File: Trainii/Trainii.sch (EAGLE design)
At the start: 29 parts, among them J1 apd, J2 left motor encoder, J3 right motor encoder, J4 line sensor 2, J5 line sensor 1, J6 ultrasonic, J7 left motor output, J8 right motor output, J9 lift motor output

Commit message: Changed a few parts, corrected small wiring connections, routed board
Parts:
- removed U$1, U$2: DRV8833, Tranii:DRV8833
- removed U$8: BSS138, Tranii:BSS138
- removed U$9: LM3671, Tranii:LM3671
- added MC1, MC2: DRV8833, Trainii:DRV8833
- added U1: TPS61222DCKR, Trainii:TPS61222DCKR
- added U2: BSS138, Trainii:BSS138
- C2: value 0.1uF -> 10µF
- C3: value 10µF -> 0.1uF
- C5: value 4.7uF -> 10uF
- U$12: device Tranii:VLS3012HBX -> Trainii:VLS3012HBX
- U$6: device Tranii:ESP32 -> Trainii:ESP32
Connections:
- net OUT1 renamed LINE_OUT_1
- net OUT2 renamed LINE_OUT_2
- net TICKLEFT renamed TICK_LEFT
- net TICKRIGHT renamed TICK_RIGHT
- removed net LEFT0: J7.1, U$1.AOUT2
- removed net LEFT1: J7.2, U$1.AOUT1
- removed net LIFT0: J9.1, U$2.AOUT1
- removed net LIFT1: J9.2, U$2.AOUT2
- removed net N$2: C6.1, U$12.P$2, U$9.FB
- removed net RIGHT0: J8.1, U$1.BOUT1
- removed net RIGHT1: J8.2, U$1.BOUT2
- removed net VCC5: J6.1, R6.1
- new net +5V: C6.1, J6.1, R6.1, U1.FB, U1.VOUT
- new net LEFT_0: J7.1, MC1.AOUT1
- new net LEFT_1: J7.2, MC1.AOUT2
- new net LIFT_0: J9.1, MC2.AOUT1
- new net LIFT_1: J9.2, MC2.AOUT2
- new net RIGHT_0: J8.1, MC1.BOUT1
- new net RIGHT_1: J8.2, MC1.BOUT2
- net GND: now also C2.2, MC1.GND, MC1.PGND, MC2.GND, MC2.PGND, U1.GND; no longer C3.2, U$1.GND, U$1.PGND, U$2.GND, U$2.PGND, U$9.GND
- net LEFT_A: now also MC1.AIN1; no longer U$1.AIN1
- net LEFT_B: now also MC1.AIN2; no longer U$1.AIN2
- net LIFT_A: now also MC2.AIN1; no longer U$2.AIN1
- net LIFT_B: now also MC2.AIN2; no longer U$2.AIN2
- net N$1: now also U1.L; no longer U$9.SW
- net N$10: now also MC1.AISEN; no longer U$1.AISEN
- net N$3: now also C3.2, MC2.VCP; no longer C2.2, U$2.VCP
- net N$4: now also MC2.BISEN; no longer U$2.BISEN
- net N$5: now also C4.1, MC2.VINT; no longer C3.1, U$2.VINT
- net N$6: now also MC2.AISEN; no longer U$2.AISEN
- net N$7: now also MC1.VCP; no longer U$1.VCP
- net N$8: now also C2.1, MC1.VINT; no longer C4.1, U$1.VINT
- net N$9: now also MC1.BISEN; no longer U$1.BISEN
- net RIGHT_A: now also MC1.BIN1; no longer U$1.BIN1
- net RIGHT_B: now also MC1.BIN2; no longer U$1.BIN2
- net TRIG: now also U2.D; no longer U$8.D
- net TRIG3.3: now also U2.S; no longer U$8.S
- net VCC: now also C3.1, MC1.NSLEEP, MC1.VM, MC2.NSLEEP, MC2.VM, U$12.P$2, U1.EN, U1.VIN, U2.G; no longer C2.1, U$1.NSLEEP, U$1.VM, U$2.NSLEEP, U$2.VM, U$8.G, U$9.EN, U$9.VIN
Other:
- moved on the sheet: C2, C3, C4, C5, C6, R5, R6

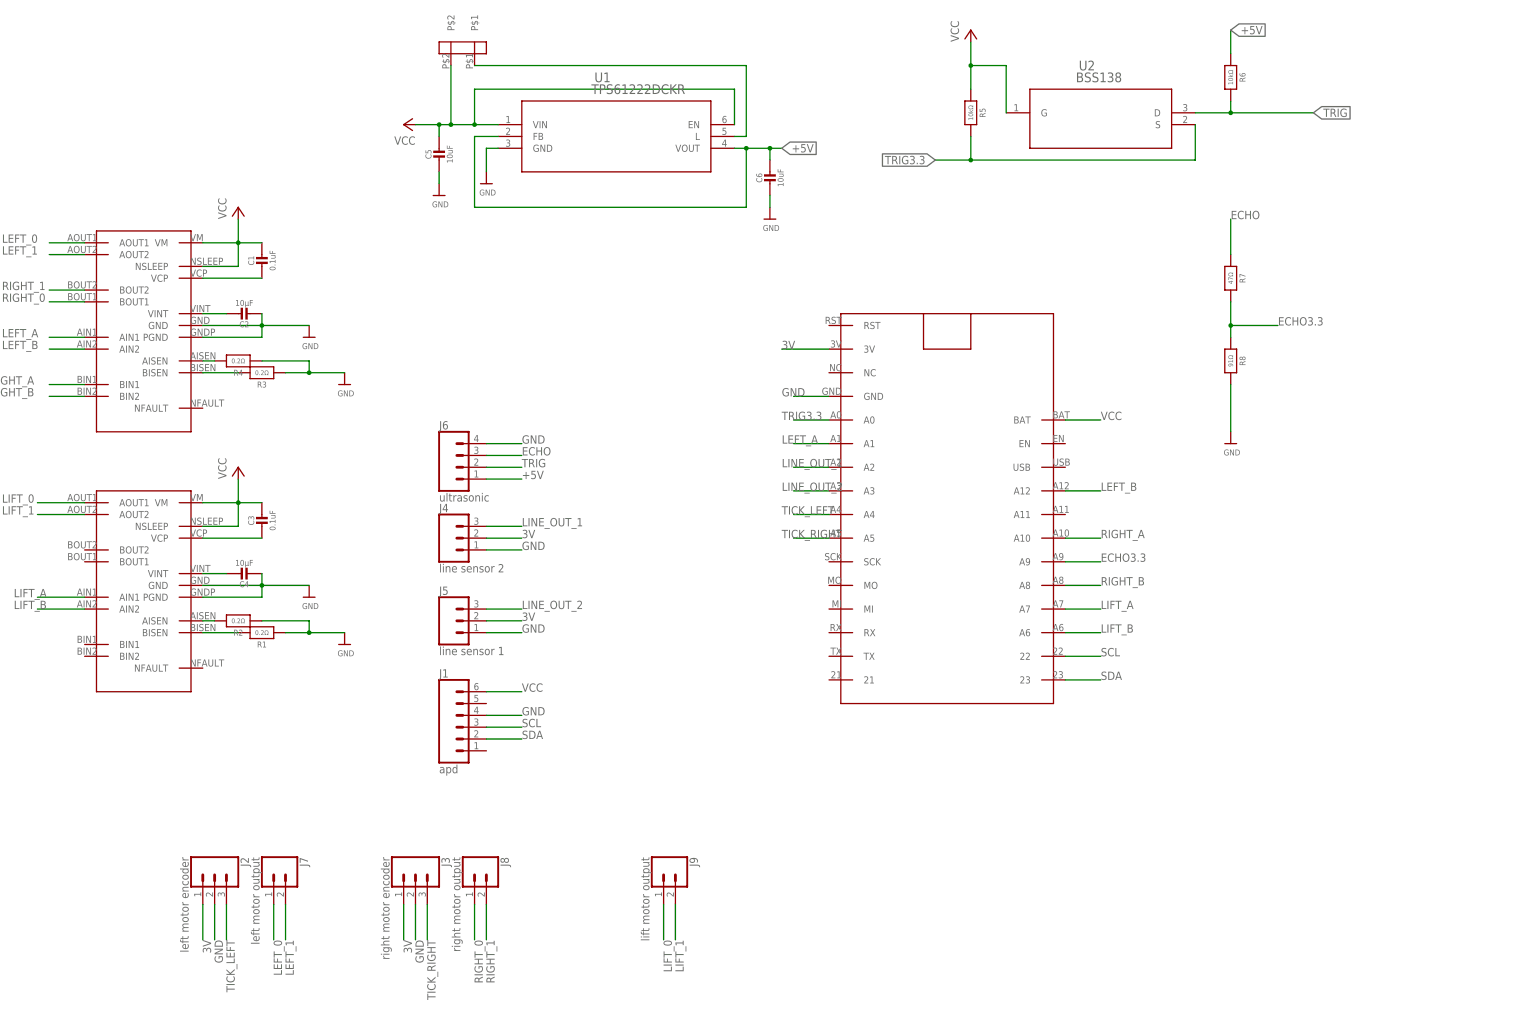
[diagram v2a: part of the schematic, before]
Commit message: Added fuse, changed power source, fixed some routing widths
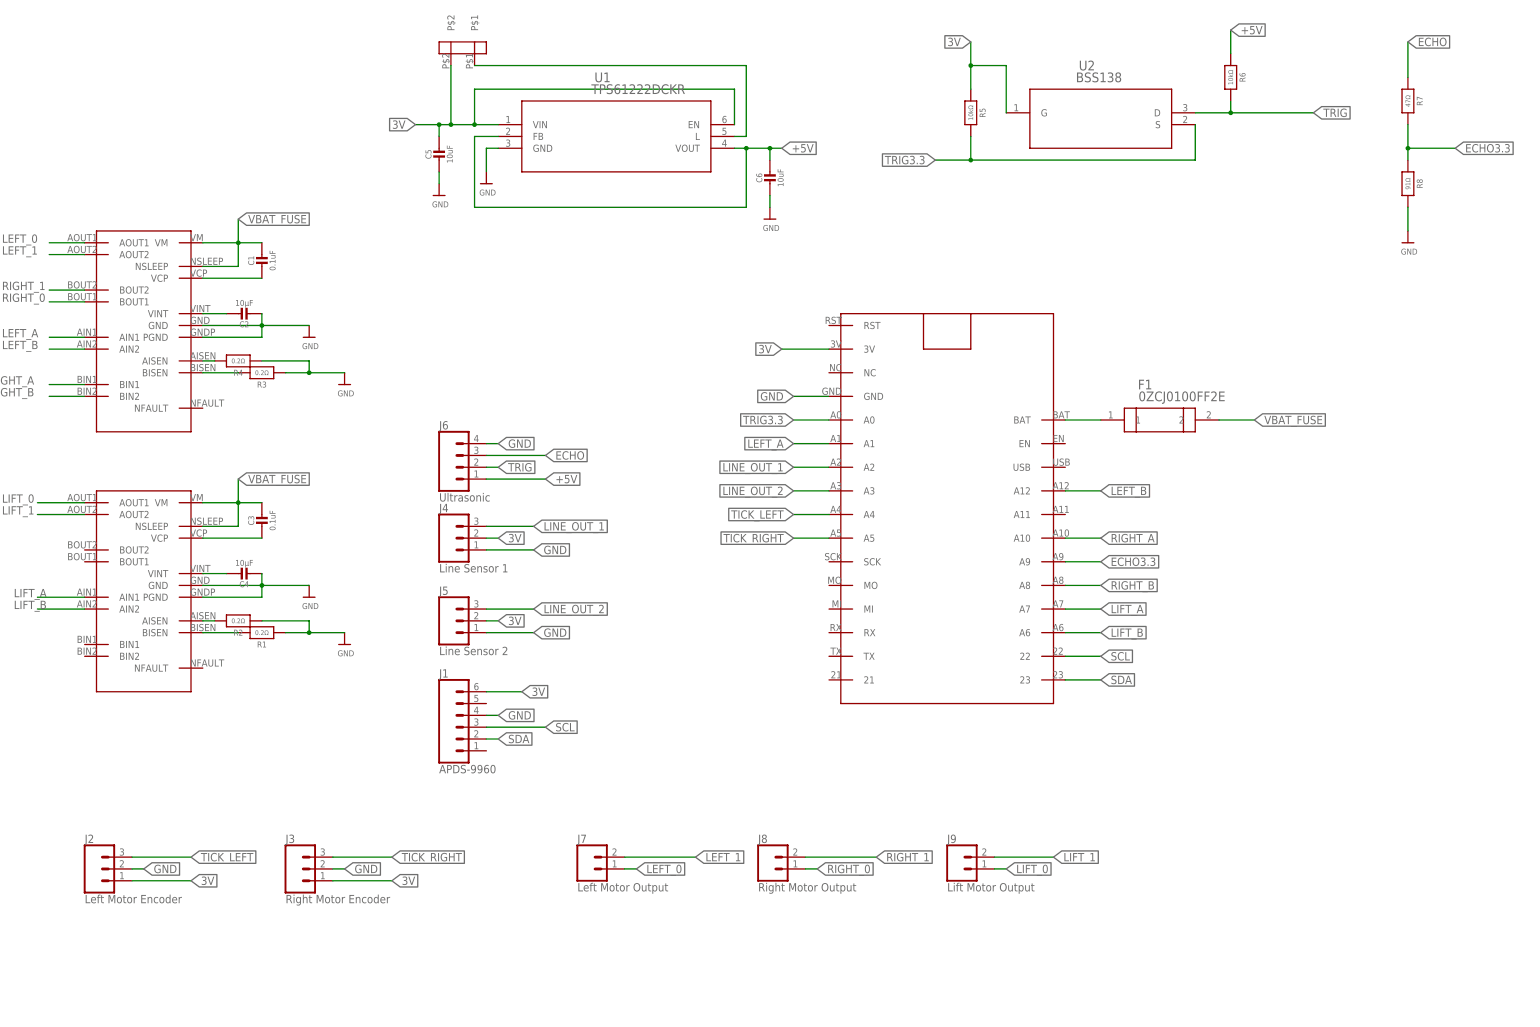
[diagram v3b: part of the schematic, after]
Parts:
- added F1: 0ZCJ0100FF2E, Trainii:0ZCJ0100FF2E
- J1: value apd -> APDS-9960
- J2: value left motor encoder -> Left Motor Encoder
- J3: value right motor encoder -> Right Motor Encoder
- J4: value line sensor 2 -> Line Sensor 1
- J5: value line sensor 1 -> Line Sensor 2
- J6: value ultrasonic -> Ultrasonic
- J7: value left motor output -> Left Motor Output
- J8: value right motor output -> Right Motor Output
- J9: value lift motor output -> Lift Motor Output
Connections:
- removed net VCC: C1.1, C3.1, C5.1, J1.6, MC1.NSLEEP, MC1.VM, MC2.NSLEEP, MC2.VM, R5.1, U$12.P$2, U$6.BAT, U1.EN, U1.VIN, U2.G
- new net VBAT: F1.1, U$6.BAT
- new net VBAT_FUSE: C1.1, C3.1, F1.2, MC1.NSLEEP, MC1.VM, MC2.NSLEEP, MC2.VM
- net 3V: now also C5.1, J1.6, R5.1, U$12.P$2, U1.EN, U1.VIN, U2.G
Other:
- moved on the sheet: J2, J3, J7, J8, J9, R7, R8

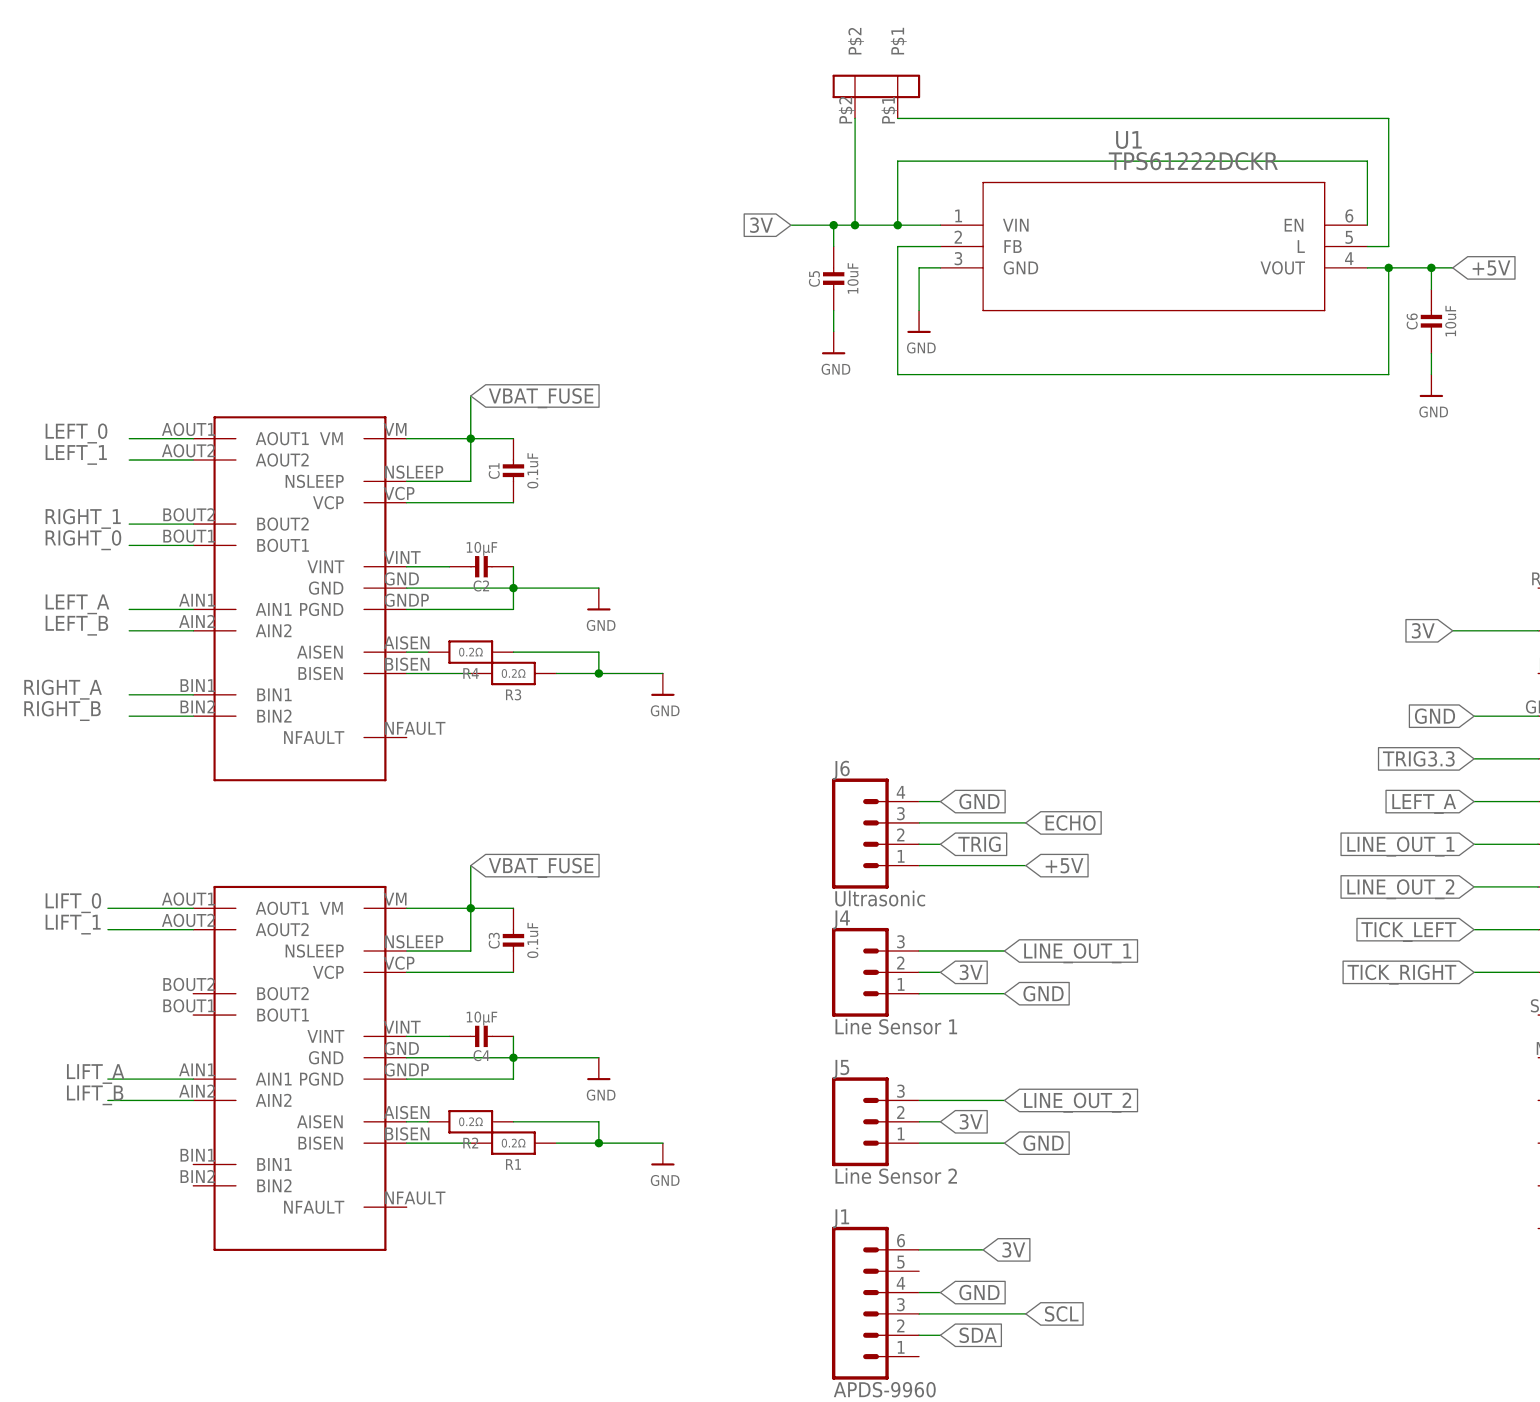
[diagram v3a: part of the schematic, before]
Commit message: Updated Library, began fixing schematic
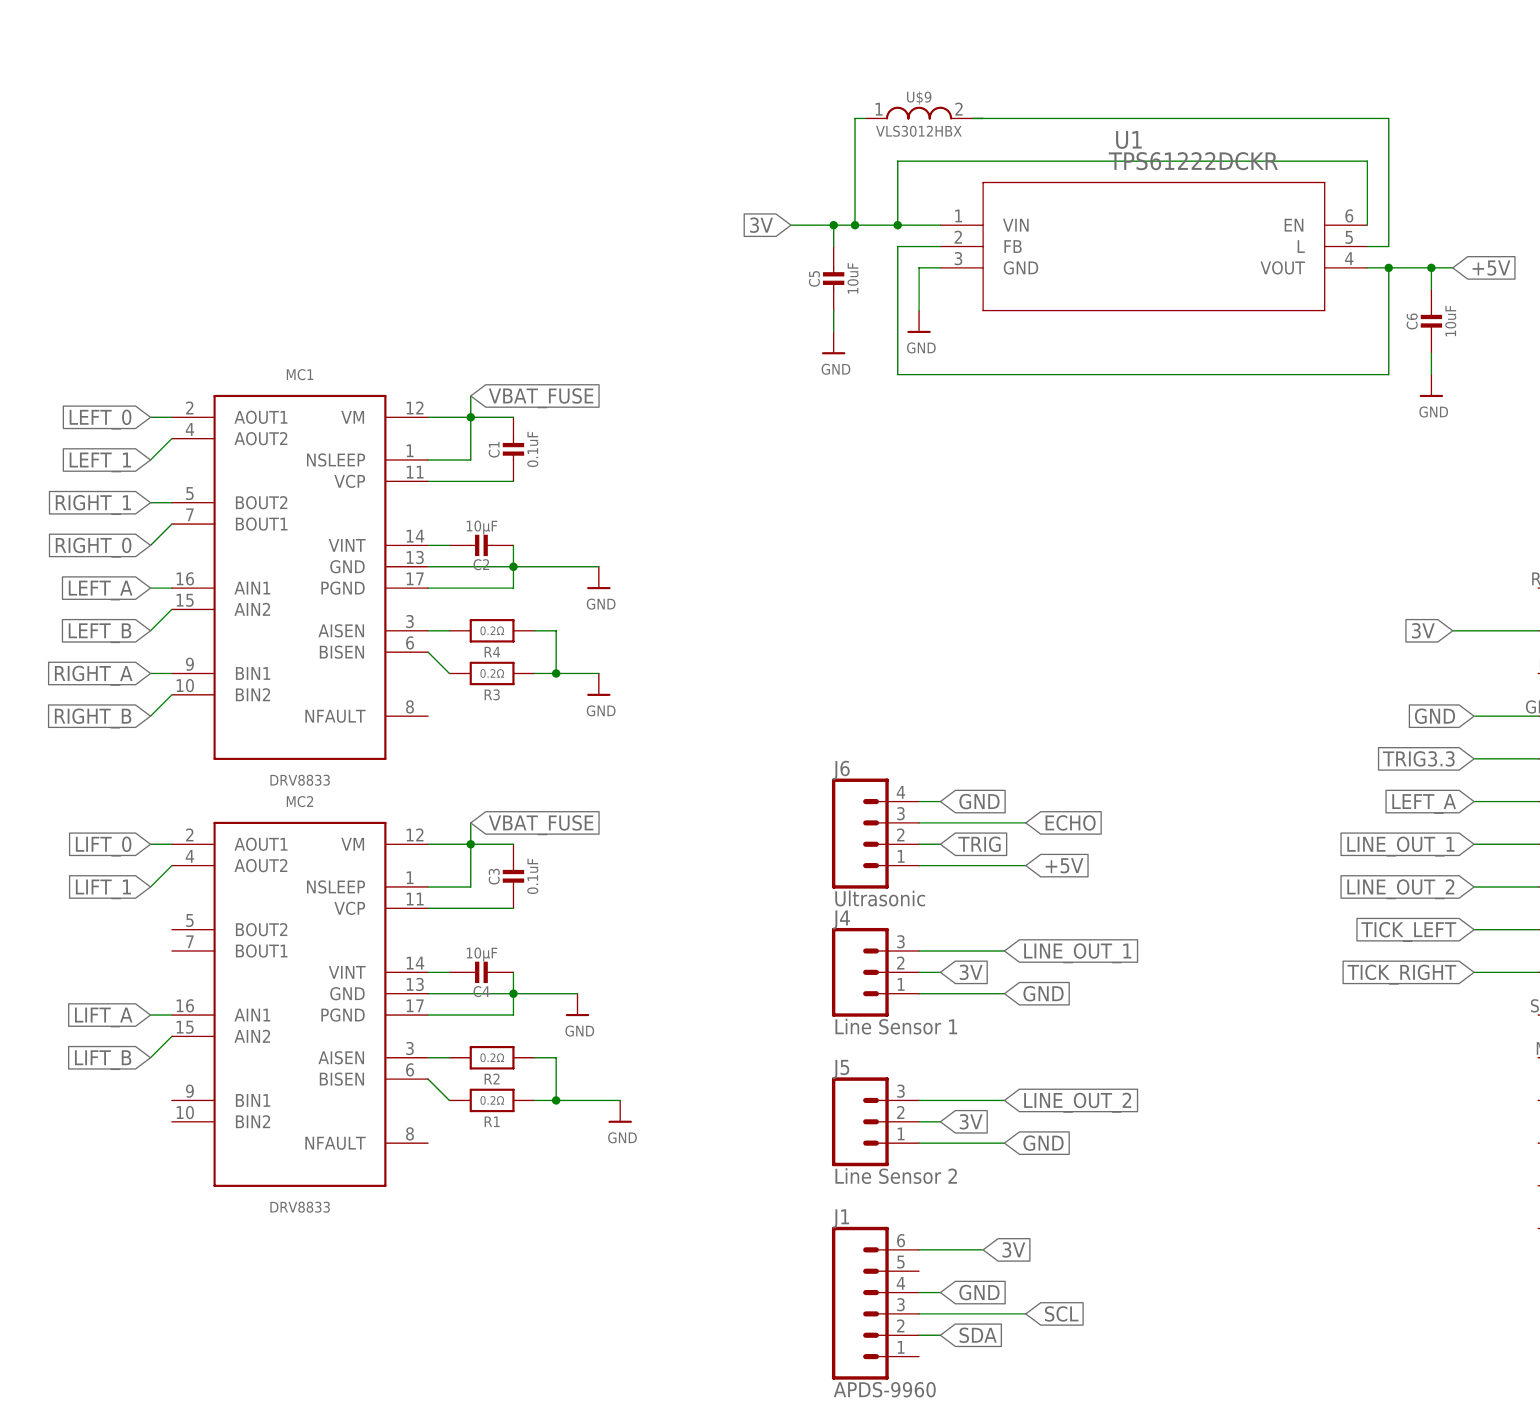
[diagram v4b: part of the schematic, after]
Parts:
- removed U$12: VLS3012HBX, Trainii:VLS3012HBX
- added U$9: VLS3012HBX, Trainii:VLS3012HBX
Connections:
- net 3V: now also U$9.IN; no longer U$12.P$2
- net N$1: now also U$9.OUT; no longer U$12.P$1
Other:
- moved on the sheet: C1, C2, C3, C4, R1, R2, R3, R4
